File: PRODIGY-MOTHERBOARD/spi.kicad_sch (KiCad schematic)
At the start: 3 parts, among them U16 TXS0108EPW

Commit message: Finished v0.1 schematic.
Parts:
- renumbered RN1 to RN3, RN2 to RN4, U16 to U13
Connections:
- no-connect marks 4 -> 5
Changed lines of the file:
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@@
+	)
+	(no_connect
+		(at 52.07 85.09)
 	)
 	(no_connect
@@
 		(dnp no)
 		(fields_autoplaced yes)
-		(property "Reference" "#PWR0121"
+		(property "Reference" "#PWR0139"
 			(at 171.45 83.82 0)
 			(effects
@@
 			(project "PRODIGY-MOTHERBOARD"
 				(path "/f1c25860-8989-4190-bd24-2491d23ca7d9/e2913798-f444-47a6-8b64-53020d7d816b"
-					(reference "#PWR0121")
+					(reference "#PWR0139")
 					(unit 1)
 				)
@@
 		(dnp no)
 		(fields_autoplaced yes)
-		(property "Reference" "#PWR0119"
+		(property "Reference" "#PWR0141"
 			(at 176.53 78.74 0)
 			(effects
@@
 			(project "PRODIGY-MOTHERBOARD"
 				(path "/f1c25860-8989-4190-bd24-2491d23ca7d9/e2913798-f444-47a6-8b64-53020d7d816b"
-					(reference "#PWR0119")
+					(reference "#PWR0141")
 					(unit 1)
 				)
@@
 		(dnp no)
 		(fields_autoplaced yes)
-		(property "Reference" "U16"
+		(property "Reference" "U13"
 			(at 176.1841 115.57 0)
 			(effects
@@
 			(project "PRODIGY-MOTHERBOARD"
 				(path "/f1c25860-8989-4190-bd24-2491d23ca7d9/e2913798-f444-47a6-8b64-53020d7d816b"
-					(reference "U16")
+					(reference "U13")
 					(unit 1)
 				)
@@
 		(dnp no)
 		(fields_autoplaced yes)
-		(property "Reference" "#PWR0118"
+		(property "Reference" "#PWR0138"
 			(at 54.61 78.74 0)
 			(effects
@@
 			(project "PRODIGY-MOTHERBOARD"
 				(path "/f1c25860-8989-4190-bd24-2491d23ca7d9/e2913798-f444-47a6-8b64-53020d7d816b"
-					(reference "#PWR0118")
+					(reference "#PWR0138")
 					(unit 1)
 				)
@@
 		(dnp no)
 		(fields_autoplaced yes)
-		(property "Reference" "#PWR0122"
+		(property "Reference" "#PWR0140"
 			(at 173.99 130.81 0)
 			(effects
@@
 			(project "PRODIGY-MOTHERBOARD"
 				(path "/f1c25860-8989-4190-bd24-2491d23ca7d9/e2913798-f444-47a6-8b64-53020d7d816b"
-					(reference "#PWR0122")
+					(reference "#PWR0140")
 					(unit 1)
 				)
@@
 		(dnp no)
 		(fields_autoplaced yes)
-		(property "Reference" "#PWR0120"
+		(property "Reference" "#PWR0142"
 			(at 194.31 78.74 0)
 			(effects
@@
 			(project "PRODIGY-MOTHERBOARD"
 				(path "/f1c25860-8989-4190-bd24-2491d23ca7d9/e2913798-f444-47a6-8b64-53020d7d816b"
-					(reference "#PWR0120")
+					(reference "#PWR0142")
 					(unit 1)
 				)
@@
 		(on_board yes)
 		(dnp no)
-		(property "Reference" "RN1"
+		(property "Reference" "RN3"
 			(at 30.734 78.486 0)
 			(effects
@@
 			(project "PRODIGY-MOTHERBOARD"
 				(path "/f1c25860-8989-4190-bd24-2491d23ca7d9/e2913798-f444-47a6-8b64-53020d7d816b"
-					(reference "RN1")
+					(reference "RN3")
 					(unit 1)
 				)
@@
 		(on_board yes)
 		(dnp no)
-		(property "Reference" "RN2"
+		(property "Reference" "RN4"
 			(at 191.77 78.9939 0)
 			(effects
@@
 			(project "PRODIGY-MOTHERBOARD"
 				(path "/f1c25860-8989-4190-bd24-2491d23ca7d9/e2913798-f444-47a6-8b64-53020d7d816b"
-					(reference "RN2")
+					(reference "RN4")
 					(unit 1)
 				)
@@
 			(project "PRODIGY-MOTHERBOARD"
 				(path "/f1c25860-8989-4190-bd24-2491d23ca7d9/e2913798-f444-47a6-8b64-53020d7d816b"
-					(page "15")
-				)
-			)
+					(page "14")
+				)
+			)

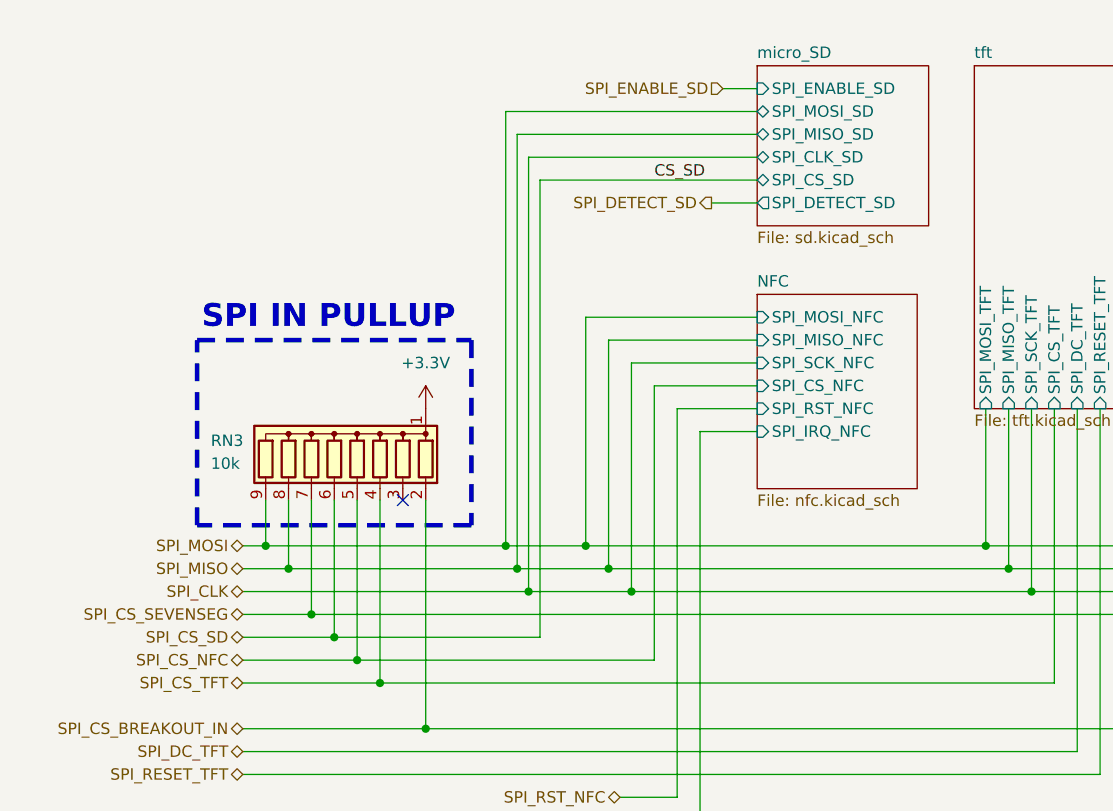
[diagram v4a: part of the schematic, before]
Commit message: MBT Schematic improved
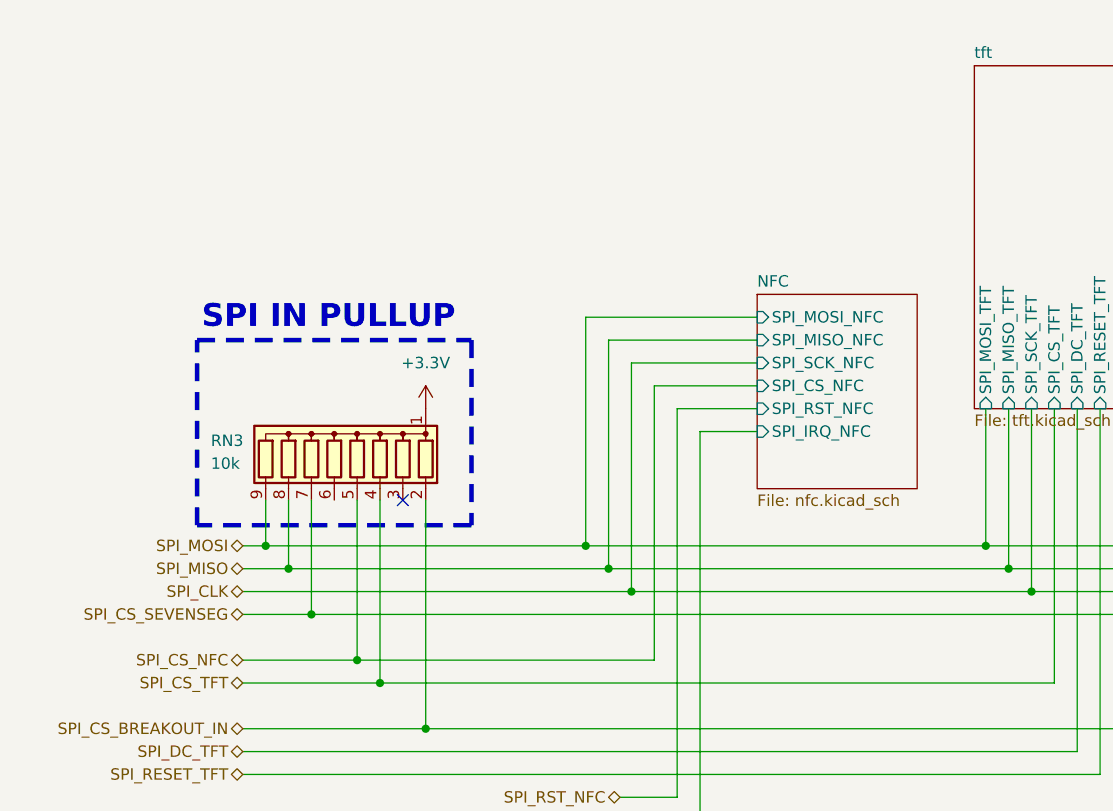
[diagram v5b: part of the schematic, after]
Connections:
- net SPI_CS_SD: no longer names the net of RN3.6 (R5)
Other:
- removed sheet micro_SD

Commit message: schematic v0.2 finalized
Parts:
- removed RN3, RN4: 10k, Resistor_SMD:R_Array_Convex_5x0603, symbol Device:R_Network08
- added RN3, RN4, RN5: 10k, Resistor_SMD:R_Array_Convex_4x0603, symbol Device:R_Network04
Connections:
- net SPI_SCK_BREAKOUT is gone; now on net SPI_MOSI_BREAKOUT: U13.17 (B3)
- net +3.3V: now also RN3.1 (common), RN4.1 (common)
- net +5V: now also RN5.1 (common)
- net CS_SEVENSEG: now also RN5.4 (R3)
- net SPI_CLK: now also RN3.3 (R2)
- net SPI_CS_BREAKOUT: now also RN5.5 (R4)
- net SPI_CS_BREAKOUT_IN: now also RN4.4 (R3)
- net SPI_CS_NFC: now also RN3.2 (R1)
- net SPI_CS_TFT: now also RN4.5 (R4)
- net SPI_MISO: now also RN3.4 (R3)
- net SPI_MISO_BREAKOUT: now also RN5.3 (R2)
- net SPI_MOSI: now also RN3.5 (R4)
- net SPI_MOSI_BREAKOUT: now also RN5.2 (R1)
- net SPI_RESET_TFT: now also RN4.3 (R2)
- net SPI_RST_NFC: now also RN4.2 (R1)
- no-connect marks 5 -> 6

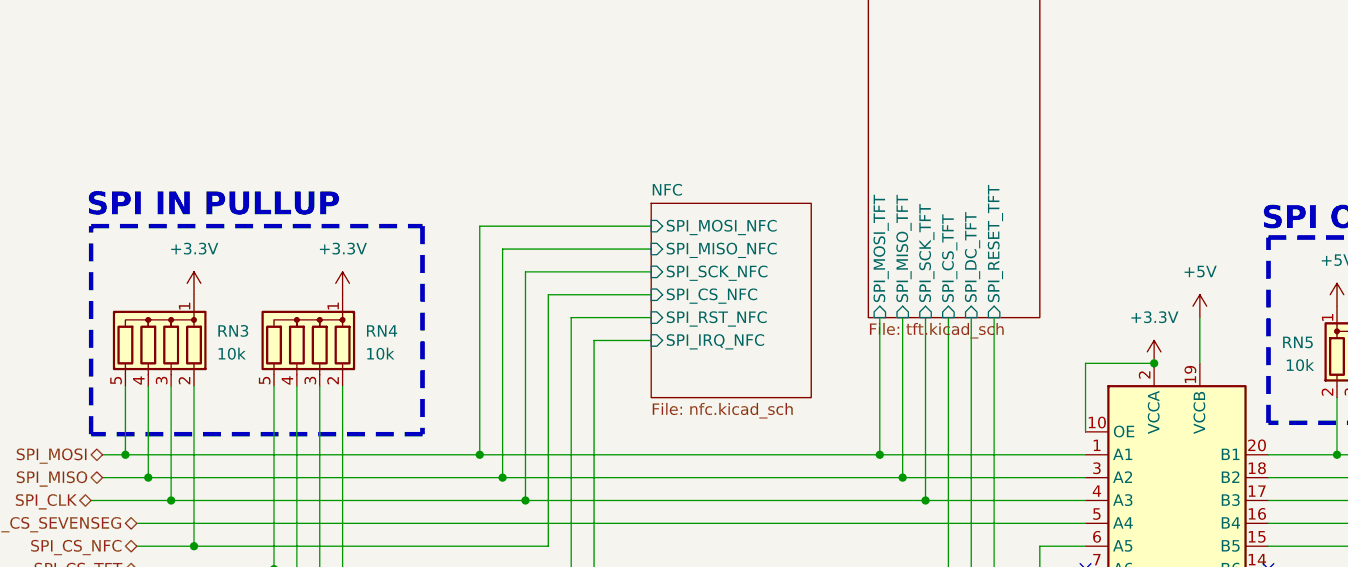
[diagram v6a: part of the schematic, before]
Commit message: Motherboard footprints assigned.
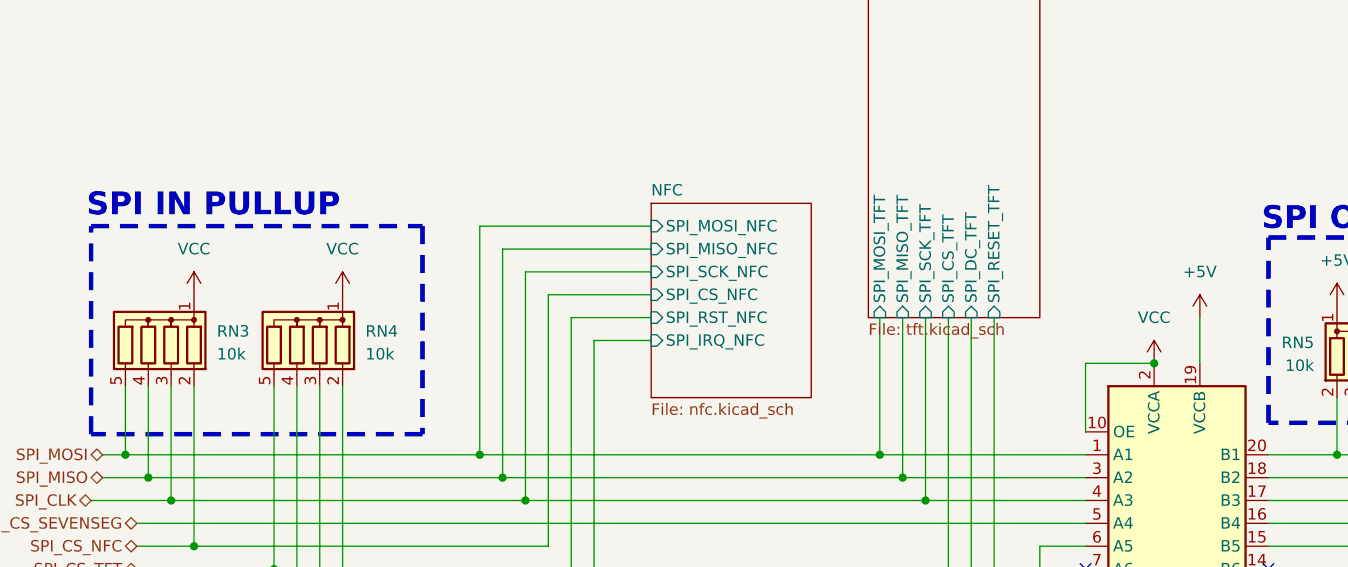
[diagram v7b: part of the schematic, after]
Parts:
- RN3, RN4, RN5: footprint Resistor_SMD:R_Array_Convex_4x0603 -> Resistor_SMD:R_0603_1608Metric
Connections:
- net +3.3V renamed VCC
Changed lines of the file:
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@@
+	)
+	(junction
+		(at 171.45 80.01)
+		(diameter 0)
+		(color 0 0 0 0)
 	)
 	(junction
@@
 	)
 	(junction
-		(at 171.45 80.01)
-		(diameter 0)
-		(color 0 0 0 0)
-	)
-	(junction
 		(at 143.51 92.71)
 		(diameter 0)
@@
 			)
 			(justify left)
-		)
-	)
-	(symbol
-		(lib_id "power:+3.3V")
-		(at 171.45 80.01 0)
-		(unit 1)
-		(exclude_from_sim no)
-		(in_bom yes)
-		(on_board yes)
-		(dnp no)
-		(fields_autoplaced yes)
-		(property "Reference" "#PWR0143"
-			(at 171.45 83.82 0)
-			(effects
-				(font
-					(size 1.27 1.27)
-				)
-				(hide yes)
-			)
-		)
-		(property "Value" "+3.3V"
-			(at 171.45 74.93 0)
-			(effects
-				(font
-					(size 1.27 1.27)
-				)
-			)
-		)
-		(property "Footprint" ""
-			(at 171.45 80.01 0)
-			(effects
-				(font
-					(size 1.27 1.27)
-				)
-				(hide yes)
-			)
-		)
-		(property "Datasheet" ""
-			(at 171.45 80.01 0)
-			(effects
-				(font
-					(size 1.27 1.27)
-				)
-				(hide yes)
-			)
-		)
-		(property "Description" "Power symbol creates a global label with name \"+3.3V\""
-			(at 171.45 80.01 0)
-			(effects
-				(font
-					(size 1.27 1.27)
-				)
-				(hide yes)
-			)
-		)
-		(pin "1"
-		)
-		(instances
-			(project "PRODIGY-MOTHERBOARD"
-				(path "/f1c25860-8989-4190-bd24-2491d23ca7d9/e2913798-f444-47a6-8b64-53020d7d816b"
-					(reference "#PWR0143")
-					(unit 1)
-				)
-			)
 		)
 	)
@@
 		)
 		(property "Description" "Bidirectional  level-shifting voltage translator, TSSOP-20"
+			(at 173.99 97.79 0)
+			(effects
+				(font
+					(size 1.27 1.27)
+				)
+				(hide yes)
+			)
+		)
+		(property "MOUSER" ""
+			(at 173.99 97.79 0)
+			(effects
+				(font
+					(size 1.27 1.27)
+				)
+				(hide yes)
+			)
+		)
+		(property "Sim.Type" ""
+			(at 173.99 97.79 0)
+			(effects
+				(font
+					(size 1.27 1.27)
+				)
+				(hide yes)
+			)
+		)
+		(property "TME" ""
 			(at 173.99 97.79 0)
 			(effects
@@
 			)
 		)
-		(property "Footprint" "Resistor_SMD:R_Array_Convex_4x0603"
+		(property "Footprint" "Resistor_SMD:R_0603_1608Metric"
 			(at 203.835 78.74 90)
 			(effects
@@
 		)
 		(property "Description" "4 resistor network, star topology, bussed resistors, small symbol"
+			(at 196.85 78.74 0)
+			(effects
+				(font
+					(size 1.27 1.27)
+				)
+				(hide yes)
+			)
+		)
+		(property "MOUSER" ""
+			(at 196.85 78.74 0)
+			(effects
+				(font
+					(size 1.27 1.27)
+				)
+				(hide yes)
+			)
+		)
+		(property "Sim.Type" ""
+			(at 196.85 78.74 0)
+			(effects
+				(font
+					(size 1.27 1.27)
+				)
+				(hide yes)
+			)
+		)
+		(property "TME" ""
 			(at 196.85 78.74 0)
 			(effects
@@
 			)
 		)
-		(property "Footprint" "Resistor_SMD:R_Array_Convex_4x0603"
+		(property "Footprint" "Resistor_SMD:R_0603_1608Metric"
 			(at 52.705 77.47 90)
 			(effects
@@
 		)
 		(property "Description" "4 resistor network, star topology, bussed resistors, small symbol"
+			(at 59.69 77.47 0)
+			(effects
+				(font
+					(size 1.27 1.27)
+				)
+				(hide yes)
+			)
+		)
+		(property "MOUSER" ""
+			(at 59.69 77.47 0)
+			(effects
+				(font
+					(size 1.27 1.27)
+				)
+				(hide yes)
+			)
+		)
+		(property "Sim.Type" ""
+			(at 59.69 77.47 0)
+			(effects
+				(font
+					(size 1.27 1.27)
+				)
+				(hide yes)
+			)
+		)
+		(property "TME" ""
 			(at 59.69 77.47 0)
 			(effects
@@
 	)
 	(symbol
-		(lib_id "power:+3.3V")
-		(at 64.77 72.39 0)
-		(unit 1)
-		(exclude_from_sim no)
-		(in_bom yes)
-		(on_board yes)
-		(dnp no)
-		(fields_autoplaced yes)
-		(property "Reference" "#PWR0141"
-			(at 64.77 76.2 0)
-			(effects
-				(font
-					(size 1.27 1.27)
-				)
-				(hide yes)
-			)
-		)
-		(property "Value" "+3.3V"
-			(at 64.77 67.31 0)
-			(effects
-				(font
-					(size 1.27 1.27)
-				)
-			)
-		)
-		(property "Footprint" ""
-			(at 64.77 72.39 0)
-			(effects
-				(font
-					(size 1.27 1.27)
-				)
-				(hide yes)
-			)
-		)
-		(property "Datasheet" ""
-			(at 64.77 72.39 0)
-			(effects
-				(font
-					(size 1.27 1.27)
-				)
-				(hide yes)
-			)
-		)
-		(property "Description" "Power symbol creates a global label with name \"+3.3V\""
-			(at 64.77 72.39 0)
-			(effects
-				(font
-					(size 1.27 1.27)
-				)
-				(hide yes)
-			)
-		)
-		(pin "1"
-		)
-		(instances
-			(project "PRODIGY-MOTHERBOARD"
-				(path "/f1c25860-8989-4190-bd24-2491d23ca7d9/e2913798-f444-47a6-8b64-53020d7d816b"
-					(reference "#PWR0141")
-					(unit 1)
-				)
-			)
-		)
-	)
-	(symbol
-		(lib_id "power:+3.3V")
+		(lib_id "power:VCC")
 		(at 81.28 72.39 0)
 		(unit 1)
@@
 			)
 		)
-		(property "Value" "+3.3V"
+		(property "Value" "VCC"
 			(at 81.28 67.31 0)
 			(effects
@@
 			)
 		)
-		(property "Description" "Power symbol creates a global label with name \"+3.3V\""
+		(property "Description" "Power symbol creates a global label with name \"VCC\""
 			(at 81.28 72.39 0)
 			(effects
@@
 				(path "/f1c25860-8989-4190-bd24-2491d23ca7d9/e2913798-f444-47a6-8b64-53020d7d816b"
 					(reference "#PWR0144")
+					(unit 1)
+				)
+			)
+		)
+	)
+	(symbol
+		(lib_id "power:VCC")
+		(at 64.77 72.39 0)
+		(unit 1)
+		(exclude_from_sim no)
+		(in_bom yes)
+		(on_board yes)
+		(dnp no)
+		(fields_autoplaced yes)
+		(property "Reference" "#PWR0141"
+			(at 64.77 76.2 0)
+			(effects
+				(font
+					(size 1.27 1.27)
+				)
+				(hide yes)
+			)
+		)
+		(property "Value" "VCC"
+			(at 64.77 67.31 0)
+			(effects
+				(font
+					(size 1.27 1.27)
+				)
+			)
+		)
+		(property "Footprint" ""
+			(at 64.77 72.39 0)
+			(effects
+				(font
+					(size 1.27 1.27)
+				)
+				(hide yes)
+			)
+		)
+		(property "Datasheet" ""
+			(at 64.77 72.39 0)
+			(effects
+				(font
+					(size 1.27 1.27)
+				)
+				(hide yes)
+			)
+		)
+		(property "Description" "Power symbol creates a global label with name \"VCC\""
+			(at 64.77 72.39 0)
+			(effects
+				(font
+					(size 1.27 1.27)
+				)
+				(hide yes)
+			)
+		)
+		(pin "1"
+		)
+		(instances
+			(project "PRODIGY-MOTHERBOARD"
+				(path "/f1c25860-8989-4190-bd24-2491d23ca7d9/e2913798-f444-47a6-8b64-53020d7d816b"
+					(reference "#PWR0141")
 					(unit 1)
 				)
@@
 			)
 		)
-		(property "Footprint" "Resistor_SMD:R_Array_Convex_4x0603"
+		(property "Footprint" "Resistor_SMD:R_0603_1608Metric"
 			(at 69.215 77.47 90)
 			(effects
@@
 		)
 		(property "Description" "4 resistor network, star topology, bussed resistors, small symbol"
+			(at 76.2 77.47 0)
+			(effects
+				(font
+					(size 1.27 1.27)
+				)
+				(hide yes)
+			)
+		)
+		(property "MOUSER" ""
+			(at 76.2 77.47 0)
+			(effects
+				(font
+					(size 1.27 1.27)
+				)
+				(hide yes)
+			)
+		)
+		(property "Sim.Type" ""
+			(at 76.2 77.47 0)
+			(effects
+				(font
+					(size 1.27 1.27)
+				)
+				(hide yes)
+			)
+		)
+		(property "TME" ""
 			(at 76.2 77.47 0)
 			(effects
@@
 					(unit 1)
 				)
+			)
+		)
+	)
+	(symbol
+		(lib_id "power:VCC")
+		(at 171.45 80.01 0)
+		(unit 1)
+		(exclude_from_sim no)
+		(in_bom yes)
+		(on_board yes)
+		(dnp no)
+		(fields_autoplaced yes)
+		(property "Reference" "#PWR0143"
+			(at 171.45 83.82 0)
+			(effects
+				(font
+					(size 1.27 1.27)
+				)
+				(hide yes)
+			)
+		)
+		(property "Value" "VCC"
+			(at 171.45 74.93 0)
+			(effects
+				(font
+					(size 1.27 1.27)
+				)
+			)
+		)
+		(property "Footprint" ""
+			(at 171.45 80.01 0)
+			(effects
+				(font
+					(size 1.27 1.27)
+				)
+				(hide yes)
+			)
+		)
+		(property "Datasheet" ""
+			(at 171.45 80.01 0)
+			(effects
+				(font
+					(size 1.27 1.27)
+				)
+				(hide yes)
+			)
+		)
+		(property "Description" "Power symbol creates a global label with name \"VCC\""
+			(at 171.45 80.01 0)
+			(effects
+				(font
+					(size 1.27 1.27)
+				)
+				(hide yes)
+			)
+		)
+		(pin "1"
+		)
+		(instances
+			(project "PRODIGY-MOTHERBOARD"
+				(path "/f1c25860-8989-4190-bd24-2491d23ca7d9/e2913798-f444-47a6-8b64-53020d7d816b"
+					(reference "#PWR0143")
+					(unit 1)
+				)

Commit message: finished motherboard bom and updated footprints
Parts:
- RN3, RN4, RN5: TME (none) -> DR1206-10K-4/8
- U13: TME (none) -> TXS0108EPWR
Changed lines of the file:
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@@
 			)
 		)
-		(property "TME" ""
+		(property "TME" "TXS0108EPWR"
 			(at 173.99 97.79 0)
 			(effects
@@
 			)
 		)
-		(property "TME" ""
+		(property "TME" "DR1206-10K-4/8"
 			(at 196.85 78.74 0)
 			(effects
@@
 			)
 		)
-		(property "TME" ""
+		(property "TME" "DR1206-10K-4/8"
 			(at 59.69 77.47 0)
 			(effects
@@
 			)
 		)
-		(property "TME" ""
+		(property "TME" "DR1206-10K-4/8"
 			(at 76.2 77.47 0)
 			(effects
